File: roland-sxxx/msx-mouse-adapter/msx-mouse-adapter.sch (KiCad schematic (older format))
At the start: 14 parts, among them J1 MSX DSUB9 Female, J2 PS/2 USB Connector, J3 PROG, U1 ATmega168PA-AU, Y1 16.000Mhz

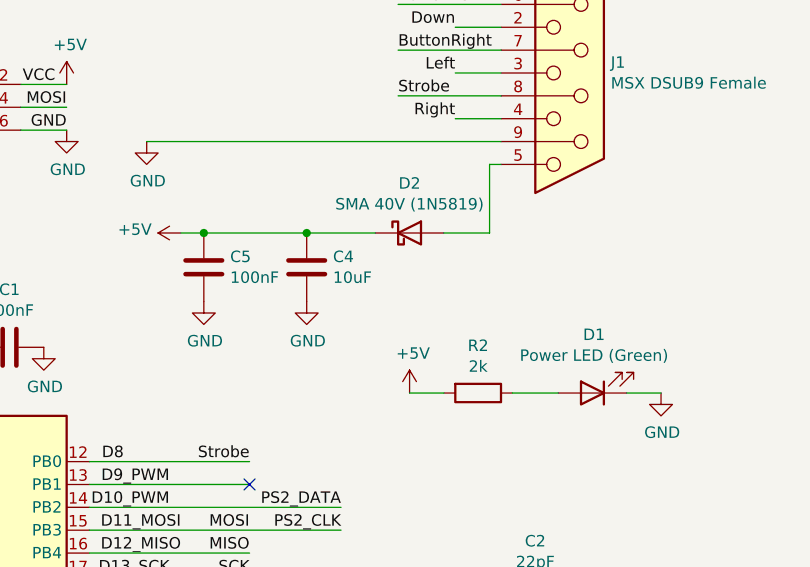
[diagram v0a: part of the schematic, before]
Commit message: made the mouse adapter more compact.
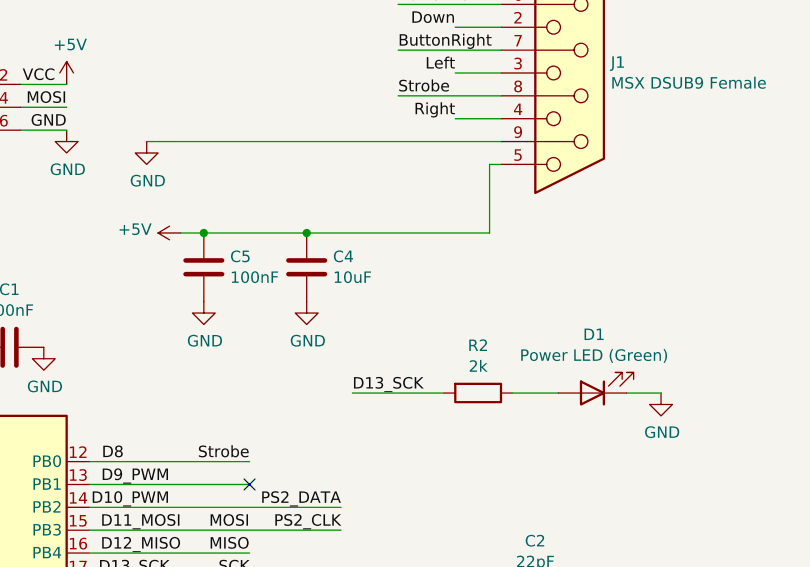
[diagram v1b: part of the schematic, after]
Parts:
- removed D2: SMA 40V (1N5819), Diode_SMD:D_SMA, symbol Device:D_Schottky
- C1, C2, C3, C5: footprint Capacitor_SMD:C_0402_1005Metric_Pad0.74x0.62mm_HandSolder -> Capacitor_SMD:C_0805_2012Metric_Pad1.18x1.45mm_HandSolder
- D1: footprint LED_SMD:LED_0402_1005Metric_Pad0.77x0.64mm_HandSolder -> LED_SMD:LED_0805_2012Metric_Pad1.15x1.40mm_HandSolder
- J1: footprint Connector_Dsub:DSUB-9_Female_Horizontal_P2.77x2.84mm_EdgePinOffset4.94mm_Housed_MountingHolesOffset7.48mm -> custom:MSX DSUB9 Female
- R1, R2: footprint Resistor_SMD:R_0402_1005Metric_Pad0.72x0.64mm_HandSolder -> Resistor_SMD:R_0805_2012Metric_Pad1.20x1.40mm_HandSolder
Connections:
- net +5V: now also J1.5; no longer R2.2
- net D13_SCK: now also R2.2
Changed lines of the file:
@@
 F 0 "C3" V 9002 5750 50  0000 C CNN
 F 1 "22pF" V 8911 5750 50  0000 C CNN
-F 2 "Capacitor_SMD:C_0402_1005Metric_Pad0.74x0.62mm_HandSolder" H 8788 5600 50  0001 C CNN
+F 2 "Capacitor_SMD:C_0805_2012Metric_Pad1.18x1.45mm_HandSolder" H 8788 5600 50  0001 C CNN
 F 3 "~" H 8750 5750 50  0001 C CNN
 F 4 "C1555" H 8750 5750 50  0001 C CNN "LCSC"
@@
 F 0 "C2" V 9002 5250 50  0000 C CNN
 F 1 "22pF" V 8911 5250 50  0000 C CNN
-F 2 "Capacitor_SMD:C_0402_1005Metric_Pad0.74x0.62mm_HandSolder" H 8788 5100 50  0001 C CNN
+F 2 "Capacitor_SMD:C_0805_2012Metric_Pad1.18x1.45mm_HandSolder" H 8788 5100 50  0001 C CNN
 F 3 "~" H 8750 5250 50  0001 C CNN
 F 4 "C1555" H 8750 5250 50  0001 C CNN "LCSC"
@@
 F 0 "R1" V 7443 6150 50  0000 C CNN
 F 1 "10k" V 7534 6150 50  0000 C CNN
-F 2 "Resistor_SMD:R_0402_1005Metric_Pad0.72x0.64mm_HandSolder" V 7580 6150 50  0001 C CNN
+F 2 "Resistor_SMD:R_0805_2012Metric_Pad1.20x1.40mm_HandSolder" V 7580 6150 50  0001 C CNN
 F 3 "~" H 7650 6150 50  0001 C CNN
 F 4 "C25744" V 7650 6150 50  0001 C CNN "LCSC"
@@
 F 0 "R2" V 8293 4350 50  0000 C CNN
 F 1 "2k" V 8384 4350 50  0000 C CNN
-F 2 "Resistor_SMD:R_0402_1005Metric_Pad0.72x0.64mm_HandSolder" V 8430 4350 50  0001 C CNN
+F 2 "Resistor_SMD:R_0805_2012Metric_Pad1.20x1.40mm_HandSolder" V 8430 4350 50  0001 C CNN
 F 3 "~" H 8500 4350 50  0001 C CNN
 F 4 "C4109" V 8500 4350 50  0001 C CNN "LCSC"
@@
 F 0 "D1" H 8993 4095 50  0000 C CNN
 F 1 "Power LED (Green)" H 8993 4186 50  0000 C CNN
-F 2 "LED_SMD:LED_0402_1005Metric_Pad0.77x0.64mm_HandSolder" H 9000 4350 50  0001 C CNN
+F 2 "LED_SMD:LED_0805_2012Metric_Pad1.15x1.40mm_HandSolder" H 9000 4350 50  0001 C CNN
 F 3 "~" H 9000 4350 50  0001 C CNN
 F 4 "C917188" H 9000 4350 50  0001 C CNN "LCSC"
@@
 	1    0    0    -1
 $EndComp
-$Comp
-L power:+5V #PWR014
-U 1 1 618A95FB
-P 8200 4350
-F 0 "#PWR014" H 8200 4200 50  0001 C CNN
-F 1 "+5V" H 8215 4523 50  0000 C CNN
-F 2 "" H 8200 4350 50  0001 C CNN
-F 3 "" H 8200 4350 50  0001 C CNN
-	1    8200 4350
-	1    0    0    -1
-$EndComp
-Wire Wire Line
-	8350 4350 8200 4350
 Wire Wire Line
 	8650 4350 8850 4350
@@
 F 0 "C1" V 6198 4150 50  0000 C CNN
 F 1 "100nF" V 6289 4150 50  0000 C CNN
-F 2 "Capacitor_SMD:C_0402_1005Metric_Pad0.74x0.62mm_HandSolder" H 6488 4000 50  0001 C CNN
+F 2 "Capacitor_SMD:C_0805_2012Metric_Pad1.18x1.45mm_HandSolder" H 6488 4000 50  0001 C CNN
 F 3 "~" H 6450 4150 50  0001 C CNN
 F 4 "C1525" V 6450 4150 50  0001 C CNN "LCSC"
@@
 F 0 "J1" H 9080 2996 50  0000 L CNN
 F 1 "MSX DSUB9 Female" H 9080 2905 50  0000 L CNN
-F 2 "Connector_Dsub:DSUB-9_Female_Horizontal_P2.77x2.84mm_EdgePinOffset4.94mm_Housed_MountingHolesOffset7.48mm" H 8900 2950 50  0001 C CNN
+F 2 "custom:MSX DSUB9 Female" H 8900 2950 50  0001 C CNN
 F 3 " ~" H 8900 2950 50  0001 C CNN
 	1    8900 2950
@@
 F 0 "C5" H 7415 3846 50  0000 L CNN
 F 1 "100nF" H 7415 3755 50  0000 L CNN
-F 2 "Capacitor_SMD:C_0402_1005Metric_Pad0.74x0.62mm_HandSolder" H 7338 3650 50  0001 C CNN
+F 2 "Capacitor_SMD:C_0805_2012Metric_Pad1.18x1.45mm_HandSolder" H 7338 3650 50  0001 C CNN
 F 3 "~" H 7300 3800 50  0001 C CNN
 F 4 "C1525" H 7300 3800 50  0001 C CNN "LCSC"
@@
 $EndComp
 Connection ~ 7750 3650
-Wire Wire Line
-	7750 3650 8050 3650
 Wire Wire Line
 	7300 3650 7750 3650
@@
 Wire Wire Line
 	8050 5250 8600 5250
-$Comp
-L Device:D_Schottky D2
-U 1 1 619B75A8
-P 8200 3650
-F 0 "D2" H 8200 3867 50  0000 C CNN
-F 1 "SMA 40V (1N5819)" H 8200 3776 50  0000 C CNN
-F 2 "Diode_SMD:D_SMA" H 8200 3650 50  0001 C CNN
-F 3 "~" H 8200 3650 50  0001 C CNN
-F 4 "C2480" H 8200 3650 50  0001 C CNN "LCSC"
-	1    8200 3650
-	1    0    0    -1
-$EndComp
 Wire Wire Line
 	8550 3350 8600 3350
@@
 	8550 3350 8550 3650
 Wire Wire Line
-	8550 3650 8350 3650
+	7750 3650 8550 3650
+Wire Wire Line
+	8350 4350 7950 4350
+Text Label 7950 4350 0    50   ~ 0
+D13_SCK
 $EndSCHEMATC
